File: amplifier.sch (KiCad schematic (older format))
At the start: 2 parts

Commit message: added mosfet and driver
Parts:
- added C?: C_4.7uF_0603_25V, Main_LIB:C_0603, symbol Main_Library:C_4.7uF_0603_25V
- added C?: C_100nF_0603_50V, MAIN_PCB_LIB:C_0603, symbol Main_Library:C_100nF_0603_50V
- added Q? (x2): Q_IRFZ44NPBF_N-Channel_Infineon, MAIN_PCB_LIB:Q_IRFZ44NPBF_Infineon, symbol Main_Library:Q_IRFZ44NPBF_N-Channel_Infineon
- added U?: U_TC4427M_Microchip, MAIN_PCB_LIB:U_8_DIP_TC4427CPA_Microchip, symbol Main_Library:U_TC4427M_Microchip
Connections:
- wire segments 7 -> 18
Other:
- moved on the sheet: J?, U?A

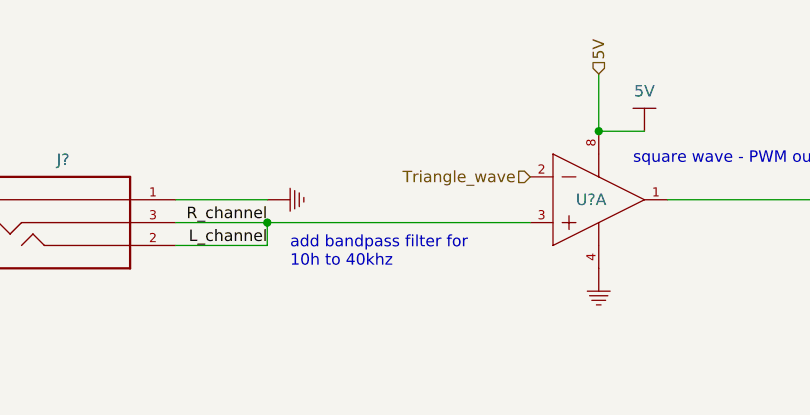
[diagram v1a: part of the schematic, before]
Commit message: added bandpass filter
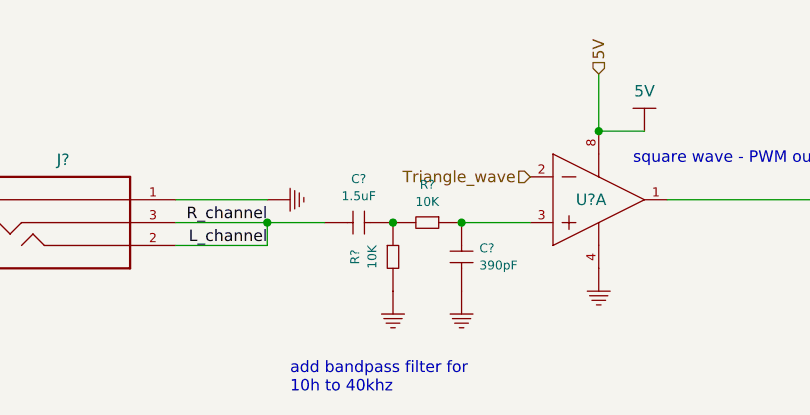
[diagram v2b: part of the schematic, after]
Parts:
- added C?: C_390pF_0603_50V, MAIN_PCB_LIB:C_0603, symbol Main_Library:C_390pF_0603_50V
- added C?: C_1.5uF_0603_25V, MAIN_PCB_LIB:C_0603, symbol Main_Library:C_1.5uF_0603_25V
- added R? (x2): R_10K_0603, Main_LIB:R_0603, symbol Main_Library:R_10K_0603
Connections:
- wire segments 18 -> 19
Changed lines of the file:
@@
 Wire Wire Line
 	3550 2900 3550 2800
-Connection ~ 3550 2800
-Wire Wire Line
-	3550 2800 4700 2800
 Text HLabel 5000 2150 1    50   Input ~ 0
 5V
@@
 Text Notes 5150 2550 0    50   ~ 0
 square wave - PWM output
-Text Notes 3650 3000 0    50   ~ 0
+Text Notes 3650 3550 0    50   ~ 0
 add bandpass filter for\n10h to 40khz
 $Comp
@@
 Wire Wire Line
 	5300 2700 6250 2700
+$Comp
+L Main_Library:R_10K_0603 R?
+U 1 1 616DB073
+P 4250 2800
+F 0 "R?" V 4084 2800 39  0000 C CNN
+F 1 "R_10K_0603" H 4200 3350 39  0001 C CNN
+F 2 "Main_LIB:R_0603" H 4250 3300 39  0001 C CNN
+F 3 "" H 4200 2950 39  0001 C CNN
+F 4 "10K" V 4159 2800 39  0000 C CNN "Waarde"
+F 5 "YAG1236CT-ND" H 4250 3400 39  0001 C CNN "Digi-key"
+	1    4250 2800
+	0    1    1    0
+$EndComp
+$Comp
+L Main_Library:R_10K_0603 R?
+U 1 1 616DCA56
+P 4100 2950
+F 0 "R?" V 3934 2950 39  0000 C CNN
+F 1 "R_10K_0603" H 4050 3500 39  0001 C CNN
+F 2 "Main_LIB:R_0603" H 4100 3450 39  0001 C CNN
+F 3 "" H 4050 3100 39  0001 C CNN
+F 4 "10K" V 4009 2950 39  0000 C CNN "Waarde"
+F 5 "YAG1236CT-ND" H 4100 3550 39  0001 C CNN "Digi-key"
+	1    4100 2950
+	1    0    0    -1
+$EndComp
+$Comp
+L Main_Library:GND #GND?
+U 1 1 616DD53E
+P 4100 3100
+F 0 "#GND?" H 3940 3080 50  0001 C CNN
+F 1 "GND" H 3940 3080 50  0001 C CNN
+F 2 "" H 4010 3040 50  0001 C CNN
+F 3 "" H 4010 3040 50  0001 C CNN
+	1    4100 3100
+	1    0    0    -1
+$EndComp
+$Comp
+L Main_Library:C_390pF_0603_50V C?
+U 1 1 616E0308
+P 4400 2950
+F 0 "C?" H 4478 2988 39  0000 L CNN
+F 1 "C_390pF_0603_50V" H 4400 3200 39  0001 C CNN
+F 2 "MAIN_PCB_LIB:C_0603" H 4450 3300 39  0001 C CNN
+F 3 "" H 4300 3000 39  0001 C CNN
+F 4 "390pF" H 4478 2913 39  0000 L CNN "Waarde"
+F 5 "399-1074-1-ND" H 4400 3250 39  0001 C CNN "Digi-Key"
+	1    4400 2950
+	1    0    0    -1
+$EndComp
+$Comp
+L Main_Library:GND #GND?
+U 1 1 616E0EA2
+P 4400 3100
+F 0 "#GND?" H 4240 3080 50  0001 C CNN
+F 1 "GND" H 4240 3080 50  0001 C CNN
+F 2 "" H 4310 3040 50  0001 C CNN
+F 3 "" H 4310 3040 50  0001 C CNN
+	1    4400 3100
+	1    0    0    -1
+$EndComp
+Wire Wire Line
+	4400 2800 4700 2800
+Connection ~ 4400 2800
+$Comp
+L Main_Library:C_1.5uF_0603_25V C?
+U 1 1 616E24B6
+P 3950 2800
+F 0 "C?" V 3759 2800 39  0000 C CNN
+F 1 "C_1.5uF_0603_25V" H 3950 3050 39  0001 C CNN
+F 2 "MAIN_PCB_LIB:C_0603" H 4000 3150 39  0001 C CNN
+F 3 "" H 3850 2850 39  0001 C CNN
+F 4 "1.5uF" V 3834 2800 39  0000 C CNN "Waarde"
+F 5 "445-5962-1-ND" H 3950 3100 39  0001 C CNN "Digi-Key"
+	1    3950 2800
+	0    1    1    0
+$EndComp
+Connection ~ 4100 2800
+Wire Wire Line
+	3550 2800 3800 2800
+Connection ~ 3550 2800
 $EndSCHEMATC

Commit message: added filter end stage
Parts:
- added C?: C_680nF_TH_450V, MAIN_PCB_LIB:C_ECWFD_Panasonic, symbol Main_Library:C_680nF_TH_450V
- added L?: L_22uH_8095_WU-TI, MAIN_PCB_LIB:L_WE-TI_8095Series, symbol Main_Library:L_22uH_8095_WU-TI
- added R? (x2): R_100K_0603, MAIN_PCB_LIB:R_0603, symbol Main_Library:R_100K_0603
- added U?: U_LM393N_NOPB, MAIN_PCB_LIB:U_TI_LM393N_NOPB, symbol Main_Library:U_LM393N_NOPB
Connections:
- net labels added: Amplifier_output, VIN
- wire segments 19 -> 29
- no-connect marks 0 -> 2
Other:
- note added: "Add decoupling?"
- note added: "add offset voltage \nto input signal"
- note added: "improve switiching add snubbing\n"
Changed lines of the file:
@@
 Text HLabel 4700 2600 0    50   Input ~ 0
 Triangle_wave
-Text Notes 5150 2550 0    50   ~ 0
+Text Notes 5000 3250 0    50   ~ 0
 square wave - PWM output
 Text Notes 3650 3550 0    50   ~ 0
@@
 L Main_Library:5V #PWR?
 U 1 1 61694913
-P 7250 2100
-F 0 "#PWR?" H 7000 2200 50  0001 C CNN
-F 1 "5V" H 7250 2275 50  0000 C CNN
-F 2 "" H 7250 2250 50  0001 C CNN
-F 3 "" H 7250 2250 50  0001 C CNN
-	1    7250 2100
+P 7600 2100
+F 0 "#PWR?" H 7350 2200 50  0001 C CNN
+F 1 "5V" H 7600 2275 50  0000 C CNN
+F 2 "" H 7600 2250 50  0001 C CNN
+F 3 "" H 7600 2250 50  0001 C CNN
+	1    7600 2100
 	1    0    0    -1
 $EndComp
@@
 	8400 3150 8400 2800
 Wire Wire Line
-	7050 2800 8400 2800
-Wire Wire Line
 	8400 2700 8400 2450
-Wire Wire Line
-	7050 2700 8400 2700
 $Comp
 L Main_Library:GND #GND?
@@
 	1    0    0    -1
 $EndComp
-Wire Wire Line
-	8700 2800 9300 2800
-Wire Wire Line
-	8700 2950 8700 2800
-Connection ~ 8700 2800
-Wire Wire Line
-	8700 2650 8700 2800
 Wire Wire Line
 	5300 2700 6250 2700
@@
 	3550 2800 3800 2800
 Connection ~ 3550 2800
+$Comp
+L Main_Library:U_LM393N_NOPB U?
+U 2 1 616DCEE6
+P 4600 3650
+F 0 "U?" H 4900 3550 50  0000 L CNN
+F 1 "U_LM393N_NOPB" H 4600 4050 50  0001 L CNN
+F 2 "MAIN_PCB_LIB:U_TI_LM393N_NOPB" H 4600 4150 50  0001 L CNN
+F 3 "" H 4600 4250 50  0001 L CNN
+F 4 "Amplifiers" H 4600 4550 50  0001 L CNN "Comp Type"
+F 5 "Datasheet URL" H 4600 4650 50  0001 L CNN "Component Link 1 Description"
+F 6 "http://www.ti.com/general/docs/lit/getliterature.tsp?genericPartNumber=LM393-N&fileType=pdf" H 4600 4750 50  0001 L CNN "Component Link 1 URL"
+F 7 "MDIP, .365 x .250 x .130in, 8 Lead, .100in Pitch" H 4600 4950 50  0001 L CNN "Package Description"
+F 8 "P0008A" H 4600 5050 50  0001 L CNN "Package Reference"
+F 9 "NSUZXYTTE#*LM*393N" H 4600 5150 50  0001 L CNN "Package Top Marking"
+F 10 "8" H 4600 5250 50  0001 L CNN "Pin Count"
+F 11 "N" H 4600 5350 50  0001 L CNN "Power Wise"
+F 12 "IC" H 4600 5450 50  0001 L CNN "category"
+F 13 "1156860" H 4600 5550 50  0001 L CNN "ciiva ids"
+F 14 "56c718e248e42434" H 4600 5650 50  0001 L CNN "library id"
+F 15 "TI National Semiconductor" H 4600 5750 50  0001 L CNN "manufacturer"
+F 16 "MS-001-BA" H 4600 5850 50  0001 L CNN "package"
+F 17 "1464069057" H 4600 5950 50  0001 L CNN "release date"
+F 18 "Yes" H 4600 6050 50  0001 L CNN "rohs"
+F 19 "5C587BB4-AF8A-4456-AC4A-BF04D6254C91" H 4600 6150 50  0001 L CNN "vault revision"
+F 20 "yes" H 4600 6250 50  0001 L CNN "imported"
+	2    4600 3650
+	1    0    0    -1
+$EndComp
+$Comp
+L Main_Library:5V #PWR?
+U 1 1 616E25EA
+P 5000 3450
+F 0 "#PWR?" H 4750 3550 50  0001 C CNN
+F 1 "5V" H 5000 3625 50  0000 C CNN
+F 2 "" H 5000 3600 50  0001 C CNN
+F 3 "" H 5000 3600 50  0001 C CNN
+	1    5000 3450
+	1    0    0    -1
+$EndComp
+Text HLabel 4700 3850 0    50   Input ~ 0
+Triangle_wave
+Wire Wire Line
+	4700 2800 4700 3650
+Connection ~ 4700 2800
+$Comp
+L Main_Library:GND #GND?
+U 1 1 616EA215
+P 5000 4050
+F 0 "#GND?" H 4840 4030 50  0001 C CNN
+F 1 "GND" H 4840 4030 50  0001 C CNN
+F 2 "" H 4910 3990 50  0001 C CNN
+F 3 "" H 4910 3990 50  0001 C CNN
+	1    5000 4050
+	1    0    0    -1
+$EndComp
+Wire Wire Line
+	5300 3750 6050 3750
+Wire Wire Line
+	6050 3750 6050 2800
+Wire Wire Line
+	6050 2800 6250 2800
+$Comp
+L Main_Library:R_100K_0603 R?
+U 1 1 616F03BF
+P 7650 3000
+F 0 "R?" H 7703 3046 50  0000 L CNN
+F 1 "R_100K_0603" H 7650 3150 50  0001 C CNN
+F 2 "MAIN_PCB_LIB:R_0603" H 7650 3150 50  0001 C CNN
+F 3 "" H 7650 3150 50  0001 C CNN
+F 4 "100K" H 7703 2955 50  0000 L CNN "Waarde"
+F 5 "603-RT0603FRE10100KL" H 7600 3300 50  0001 C CNN "Mouser"
+	1    7650 3000
+	1    0    0    -1
+$EndComp
+$Comp
+L Main_Library:R_100K_0603 R?
+U 1 1 616F1C11
+P 7950 3000
+F 0 "R?" H 8003 3046 50  0000 L CNN
+F 1 "R_100K_0603" H 7950 3150 50  0001 C CNN
+F 2 "MAIN_PCB_LIB:R_0603" H 7950 3150 50  0001 C CNN
+F 3 "" H 7950 3150 50  0001 C CNN
+F 4 "100K" H 8003 2955 50  0000 L CNN "Waarde"
+F 5 "603-RT0603FRE10100KL" H 7900 3300 50  0001 C CNN "Mouser"
+	1    7950 3000
+	1    0    0    -1
+$EndComp
+Wire Wire Line
+	7050 2700 7650 2700
+Wire Wire Line
+	7950 2850 7950 2800
+Connection ~ 7950 2800
+Wire Wire Line
+	7950 2800 8400 2800
+Wire Wire Line
+	7050 2800 7950 2800
+Wire Wire Line
+	7650 2850 7650 2700
+Connection ~ 7650 2700
+Wire Wire Line
+	7650 2700 8400 2700
+$Comp
+L Main_Library:GND #GND?
+U 1 1 616FB15D
+P 7650 3150
+F 0 "#GND?" H 7490 3130 50  0001 C CNN
+F 1 "GND" H 7490 3130 50  0001 C CNN
+F 2 "" H 7560 3090 50  0001 C CNN
+F 3 "" H 7560 3090 50  0001 C CNN
+	1    7650 3150
+	1    0    0    -1
+$EndComp
+$Comp
+L Main_Library:GND #GND?
+U 1 1 616FB8AE
+P 7950 3150
+F 0 "#GND?" H 7790 3130 50  0001 C CNN
+F 1 "GND" H 7790 3130 50  0001 C CNN
+F 2 "" H 7860 3090 50  0001 C CNN
+F 3 "" H 7860 3090 50  0001 C CNN
+	1    7950 3150
+	1    0    0    -1
+$EndComp
+NoConn ~ 7050 2900
+NoConn ~ 6250 2600
+Text HLabel 8700 2050 1    50   Input ~ 0
+VIN
+Wire Wire Line
+	8700 2050 8700 2250
+$Comp
+L Main_Library:C_680nF_TH_450V C?
+U 1 1 6170D4C2
+P 9300 2950
+F 0 "C?" H 9378 2996 50  0000 L CNN
+F 1 "C_680nF_TH_450V" H 9350 3300 50  0001 C CNN
+F 2 "MAIN_PCB_LIB:C_ECWFD_Panasonic" H 9350 3300 50  0001 C CNN
+F 3 "" H 9200 3000 50  0001 C CNN
+F 4 "680nF" H 9378 2905 50  0000 L CNN "Waarde"
+F 5 "667-ECW-FD2W684J" H 9350 3300 50  0001 C CNN "Mouser"
+	1    9300 2950
+	1    0    0    -1
+$EndComp
+$Comp
+L Main_Library:GND #GND?
+U 1 1 6170EAC5
+P 9300 3100
+F 0 "#GND?" H 9140 3080 50  0001 C CNN
+F 1 "GND" H 9140 3080 50  0001 C CNN
+F 2 "" H 9210 3040 50  0001 C CNN
+F 3 "" H 9210 3040 50  0001 C CNN
+	1    9300 3100
+	1    0    0    -1
+$EndComp
+Wire Wire Line
+	9300 2800 9650 2800
+Wire Wire Line
+	8700 2650 8700 2800
+$Comp
+L Main_Library:L_22uH_8095_WU-TI L?
+U 1 1 61713D2D
+P 9050 2800
+F 0 "L?" H 9050 3015 50  0000 C CNN
+F 1 "L_22uH_8095_WU-TI" H 8950 3200 50  0001 C CNN
+F 2 "MAIN_PCB_LIB:L_WE-TI_8095Series" H 8900 3100 50  0001 C CNN
+F 3 "" H 8850 2850 50  0001 C CNN
+F 4 "22uH" H 9050 2924 50  0000 C CNN "Waarde"
+F 5 "710-7447720220" H 9100 3000 50  0001 C CNN "Mouser"
+	1    9050 2800
+	1    0    0    -1
+$EndComp
+Connection ~ 9300 2800
+Wire Wire Line
+	8700 2800 8800 2800
+Connection ~ 8700 2800
+Wire Wire Line
+	8700 2800 8700 2950
+Text HLabel 9650 2800 2    50   Output ~ 0
+Amplifier_output
+Connection ~ 7600 2100
+Text Notes 5050 2500 0    50   ~ 0
+Add decoupling?
+Text Notes 8750 3350 0    50   ~ 0
+improve switiching add snubbing\n
+Text Notes 3200 3100 0    50   ~ 0
+add offset voltage \nto input signal
 $EndSCHEMATC

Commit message: created pcb
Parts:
- removed U?: LM393N_NOPB, TI_National_Semiconductor-LM393N_NOPB-*, symbol Main_Library:LM393N_NOPB
- removed U?: U_LM393N_NOPB, MAIN_PCB_LIB:U_TI_LM393N_NOPB, symbol Main_Library:U_LM393N_NOPB
- added U4: U_LM393N_NOPB, MAIN_PCB_LIB:U_TI_LM393N_NOPB, symbol Main_Library:U_LM393N_NOPB
- C5: renamed from C?; footprint Main_LIB:C_0603 -> MAIN_PCB_LIB:C_0603
- J2: renamed from J?; footprint CUI_SJ1-3523N -> MAIN_PCB_LIB:J_3.5mm_JACK_CUI_SJ1-3523N
- R6, R7: renamed from R?; footprint Main_LIB:R_0603 -> MAIN_PCB_LIB:R_0603
- gave numbers to parts that had none: 10
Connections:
- net 5V: now also U4.8 (V+)
- net Triangle_wave: now also U4.2 (INA-), U4.5 (INB+)
- net at U5.2 (IN_A): now also U4.1 (OUTA)
- net at C4.1, R7.1: now also U4.3 (INA+), U4.6 (INB-)
- net at U5.4 (IN_B): now also U4.7 (OUTB)
